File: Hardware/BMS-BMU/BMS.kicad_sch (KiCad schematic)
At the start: 5 parts, among them J1 Conn_01x02, J2 Conn_01x04, J3 Conn_01x02, J4 Conn_01x03

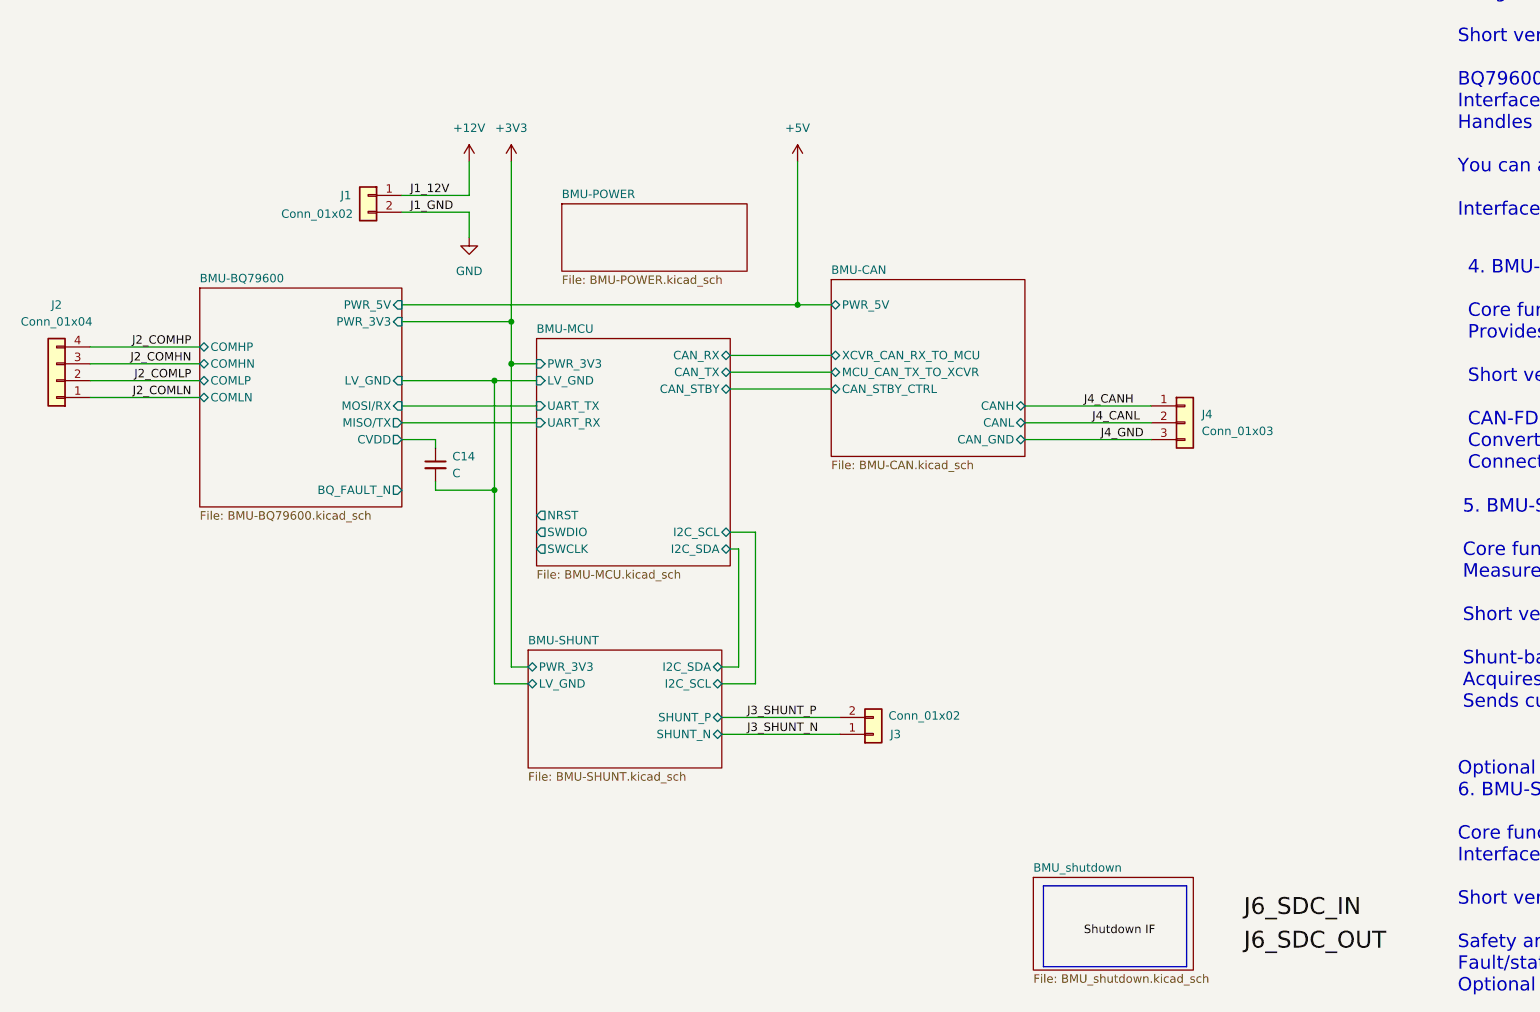
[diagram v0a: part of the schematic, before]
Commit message: update CAN and SHUNT IF
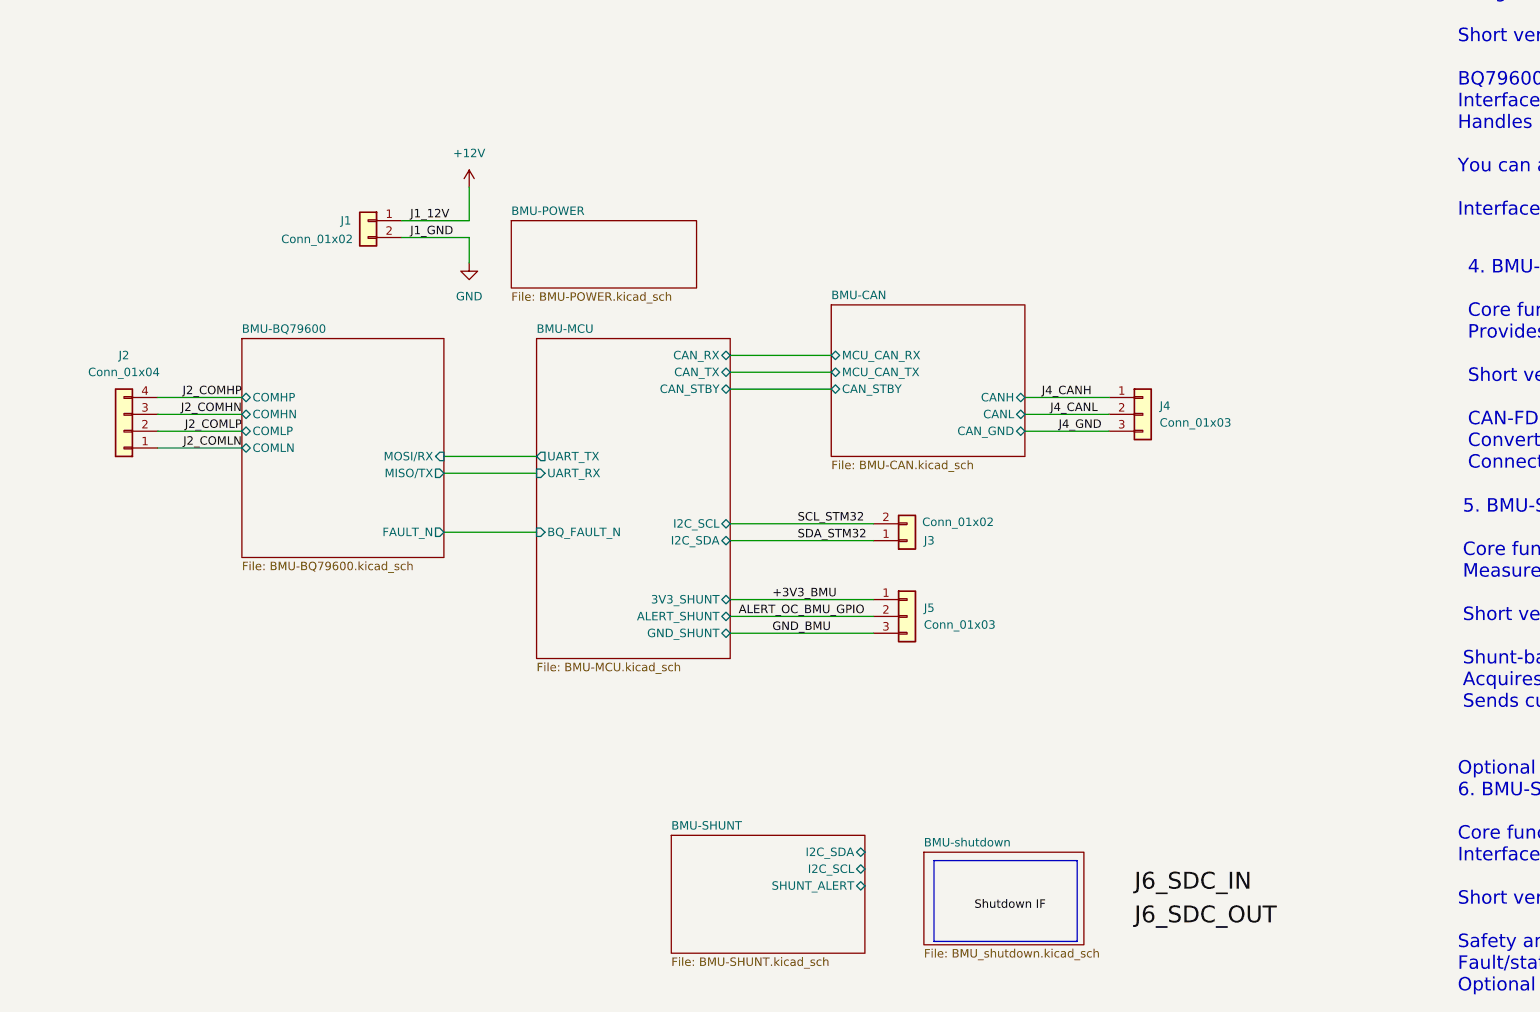
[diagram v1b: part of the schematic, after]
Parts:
- removed C14: C, symbol Device:C_Small
- added J5: Conn_01x03, symbol Connector_Generic:Conn_01x03
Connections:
- net J3_SHUNT_N renamed SDA_STM32
- net J3_SHUNT_P renamed SCL_STM32
- new net +3V3_BMU: J5.1 (Pin_1)
- new net ALERT_OC_BMU_GPIO: J5.2 (Pin_2)
- new net GND_BMU: J5.3 (Pin_3)
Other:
- sheet BMU_shutdown renamed BMU-shutdown
- sheet BMU-BQ79600 ports: added FAULT_N; removed BQ_FAULT_N, CVDD, LV_GND, PWR_3V3, PWR_5V
- sheet BMU-CAN ports: added CAN_STBY, MCU_CAN_RX, MCU_CAN_TX; removed CAN_STBY_CTRL, MCU_CAN_TX_TO_XCVR, PWR_5V, XCVR_CAN_RX_TO_MCU
- sheet BMU-MCU ports: added 3V3_SHUNT, ALERT_SHUNT, BQ_FAULT_N, GND_SHUNT; removed LV_GND, NRST, PWR_3V3, SWCLK, SWDIO
- sheet BMU-SHUNT ports: added SHUNT_ALERT; removed LV_GND, PWR_3V3, SHUNT_N, SHUNT_P
- moved on the sheet: J1, J4
